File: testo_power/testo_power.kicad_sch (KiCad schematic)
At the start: 2 parts, among them J1 USB_C_Receptacle_PowerOnly_6P, U1 74AHC240

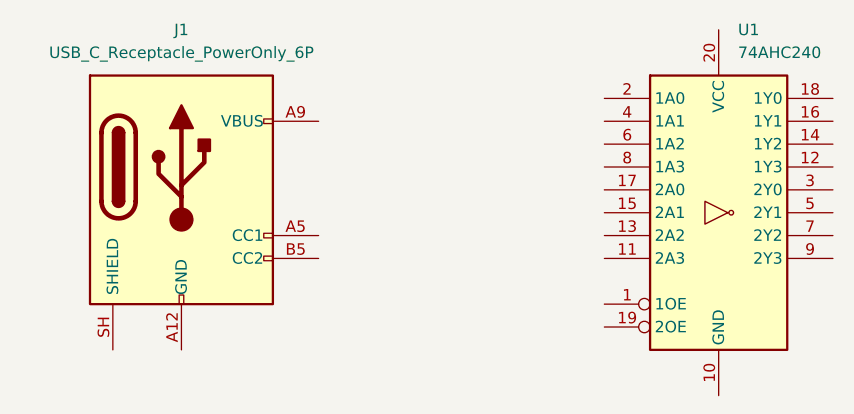
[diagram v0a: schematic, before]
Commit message: Remove useless component
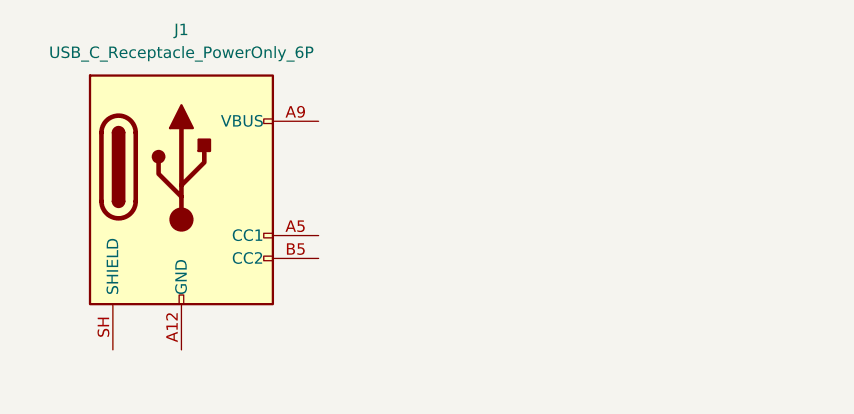
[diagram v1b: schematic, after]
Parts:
- removed U1: 74AHC240, symbol 74xx:74AHC240
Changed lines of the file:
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@@
 	(paper "A4")
-	(symbol
-		(lib_id "74xx:74AHC240")
-		(at 134.62 73.66 0)
-		(unit 1)
-		(body_style 1)
-		(exclude_from_sim no)
-		(in_bom yes)
-		(on_board yes)
-		(in_pos_files yes)
-		(dnp no)
-		(fields_autoplaced yes)
-		(property "Reference" "U1"
-			(at 136.7633 53.34 0)
-			(show_name no)
-			(do_not_autoplace no)
-			(effects
-				(font
-					(size 1.27 1.27)
-				)
-				(justify left)
-			)
-		)
-		(property "Value" "74AHC240"
-			(at 136.7633 55.88 0)
-			(show_name no)
-			(do_not_autoplace no)
-			(effects
-				(font
-					(size 1.27 1.27)
-				)
-				(justify left)
-			)
-		)
-		(property "Footprint" ""
-			(at 134.62 73.66 0)
-			(hide yes)
-			(show_name no)
-			(do_not_autoplace no)
-			(effects
-				(font
-					(size 1.27 1.27)
-				)
-			)
-		)
-		(property "Datasheet" "https://www.ti.com/lit/ds/symlink/sn54ahc240.pdf"
-			(at 134.62 73.66 0)
-			(hide yes)
-			(show_name no)
-			(do_not_autoplace no)
-			(effects
-				(font
-					(size 1.27 1.27)
-				)
-			)
-		)
-		(property "Description" "8-bit Buffer/Line Driver 3-state Inverting"
-			(at 134.62 73.66 0)
-			(hide yes)
-			(show_name no)
-			(do_not_autoplace no)
-			(effects
-				(font
-					(size 1.27 1.27)
-				)
-			)
-		)
-		(pin "14"
-		)
-		(pin "15"
-		)
-		(pin "10"
-		)
-		(pin "13"
-		)
-		(pin "8"
-		)
-		(pin "12"
-		)
-		(pin "11"
-		)
-		(pin "19"
-		)
-		(pin "7"
-		)
-		(pin "4"
-		)
-		(pin "6"
-		)
-		(pin "3"
-		)
-		(pin "5"
-		)
-		(pin "2"
-		)
-		(pin "1"
-		)
-		(pin "20"
-		)
-		(pin "17"
-		)
-		(pin "18"
-		)
-		(pin "16"
-		)
-		(pin "9"
-		)
-		(instances
-			(project "testo_power"
-				(path "/7d8517b7-4e53-4e94-8436-66e52bec9654"
-					(reference "U1")
-					(unit 1)
-				)
-			)
-		)
-	)
 	(symbol
 		(lib_id "Connector:USB_C_Receptacle_PowerOnly_6P")

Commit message: added random component
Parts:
- added U1: 74AHC240, symbol 74xx:74AHC240
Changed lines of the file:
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@@
 	(paper "A4")
+	(symbol
+		(lib_id "74xx:74AHC240")
+		(at 134.62 73.66 0)
+		(unit 1)
+		(body_style 1)
+		(exclude_from_sim no)
+		(in_bom yes)
+		(on_board yes)
+		(in_pos_files yes)
+		(dnp no)
+		(fields_autoplaced yes)
+		(property "Reference" "U1"
+			(at 136.7633 53.34 0)
+			(show_name no)
+			(do_not_autoplace no)
+			(effects
+				(font
+					(size 1.27 1.27)
+				)
+				(justify left)
+			)
+		)
+		(property "Value" "74AHC240"
+			(at 136.7633 55.88 0)
+			(show_name no)
+			(do_not_autoplace no)
+			(effects
+				(font
+					(size 1.27 1.27)
+				)
+				(justify left)
+			)
+		)
+		(property "Footprint" ""
+			(at 134.62 73.66 0)
+			(hide yes)
+			(show_name no)
+			(do_not_autoplace no)
+			(effects
+				(font
+					(size 1.27 1.27)
+				)
+			)
+		)
+		(property "Datasheet" "https://www.ti.com/lit/ds/symlink/sn54ahc240.pdf"
+			(at 134.62 73.66 0)
+			(hide yes)
+			(show_name no)
+			(do_not_autoplace no)
+			(effects
+				(font
+					(size 1.27 1.27)
+				)
+			)
+		)
+		(property "Description" "8-bit Buffer/Line Driver 3-state Inverting"
+			(at 134.62 73.66 0)
+			(hide yes)
+			(show_name no)
+			(do_not_autoplace no)
+			(effects
+				(font
+					(size 1.27 1.27)
+				)
+			)
+		)
+		(pin "14"
+		)
+		(pin "15"
+		)
+		(pin "10"
+		)
+		(pin "13"
+		)
+		(pin "8"
+		)
+		(pin "12"
+		)
+		(pin "11"
+		)
+		(pin "19"
+		)
+		(pin "7"
+		)
+		(pin "4"
+		)
+		(pin "6"
+		)
+		(pin "3"
+		)
+		(pin "5"
+		)
+		(pin "2"
+		)
+		(pin "1"
+		)
+		(pin "20"
+		)
+		(pin "17"
+		)
+		(pin "18"
+		)
+		(pin "16"
+		)
+		(pin "9"
+		)
+		(instances
+			(project "testo_power"
+				(path "/7d8517b7-4e53-4e94-8436-66e52bec9654"
+					(reference "U1")
+					(unit 1)
+				)
+			)
+		)
+	)
 	(symbol
 		(lib_id "Connector:USB_C_Receptacle_PowerOnly_6P")
